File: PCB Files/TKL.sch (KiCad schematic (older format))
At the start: 486 parts, among them J1 USB_C, SW1 ESC, SW10 F9, SW100 RGUI_R2, SW101 RCTRL_R2, SW102 STEPPED_CAPS, SW103 RSHFT_175, SW104 Fn, SW105 BKSP_2U, SW11 F10, SW12 F11, SW13 F12, SW14 PRTSC, SW15 SCRLCK, SW16 PAUSE, SW17 GRV, SW18 1, SW19 2, SW2 F1, SW20 3, SW21 4, SW22 5, SW23 6, SW24 7, SW25 8, SW26 9, SW27 0, SW28 HIFEN, SW29 PLUS, SW3 F2, SW30 BCKSLSH, SW31 DEL, SW32 INS, SW33 HOME, SW34 PGUP, SW35 TAB, SW36 Q, SW37 W, SW38 E, SW39 R, SW4 F3, SW40 T, SW41 Y, SW42 U, SW43 I, SW44 O, SW45 P, SW46 LBRACES, SW47 RBRACES, SW48 BKSP_150, SW49 DEL, SW5 F4, SW50 END, SW51 PGDN, SW52 CAPS, SW53 A, SW54 S, SW55 D, SW56 F, SW57 G, SW58 H, SW59 J, SW6 F5, SW60 K, SW61 L, SW62 :, SW63 QUOTE, SW64 ENTER, SW65 LSHFT, SW66 Z, SW67 X, SW68 C, SW69 V, SW7 F6, SW70 B, SW71 N, SW72 M, SW73 <,, SW74 .>, SW75 /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

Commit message: Added TGB fourth row to schematic
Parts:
- added C52, C53, C54, C55, C56, C57, C58, C59, C60, C61, C62, C63, C64, C65: 100nF, Capacitor_SMD:C_0805_2012Metric, symbol Device:C_Small
- added L52, L53, L54, L55, L56, L57, L58, L59, L60, L61, L62, L63, L64, L65: LED_BGRA, acheron_Components:LED_RGB_SMD_6028_2.8x3.5mm_Round, symbol Device:LED_BGRA
- added R52, R53, R54, R55, R56, R57, R58, R59, R60, R61, R62, R63, R64, R65: 100R, Resistor_SMD:R_0805_2012Metric, symbol Device:R_Small
- added RD52, RD53, RD54, RD55, RD56, RD57, RD58, RD59, RD60, RD61, RD62, RD63, RD64, RD65: 33R, Resistor_SMD:R_0805_2012Metric, symbol Device:R_Small
- added U52, U53, U54, U55, U56, U57, U58, U59, U60, U61, U62, U63, U64, U65: WS2811M, acheron_Components:MSOP-8-1EP_3x3mm_P0.65mm_EP1.68x1.88mm, symbol acheronSymbols:WS2811M
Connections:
- net 5V: now also L52.4 (A), L53.4 (A), L54.4 (A), L55.4 (A), L56.4 (A), L57.4 (A), L58.4 (A), L59.4 (A), L60.4 (A), L61.4 (A), L62.4 (A), L63.4 (A), L64.4 (A), L65.4 (A), R52.1, R53.1, R54.1, R55.1, R56.1, R57.1, R58.1, R59.1, R60.1, R61.1, R62.1, R63.1, R64.1, R65.1
- net GND: now also C52.2, C53.2, C54.2, C55.2, C56.2, C57.2, C58.2, C59.2, C60.2, C61.2, C62.2, C63.2, C64.2, C65.2, U52.4 (GND), U52.9 (GND), U53.4 (GND), U53.9 (GND), U54.4 (GND), U54.9 (GND), U55.4 (GND), U55.9 (GND), U56.4 (GND), U56.9 (GND), U57.4 (GND), U57.9 (GND), U58.4 (GND), U58.9 (GND), U59.4 (GND), U59.9 (GND), U60.4 (GND), U60.9 (GND), U61.4 (GND), U61.9 (GND), U62.4 (GND), U62.9 (GND), U63.4 (GND), U63.9 (GND), U64.4 (GND), U64.9 (GND), U65.4 (GND), U65.9 (GND)
- net at U51.5 (DO): now also RD65.2
- new net: L65.3 (RK), U65.1 (OUTR)
- new net: L65.2 (GK), U65.2 (OUTG)
- new net: L65.1 (BK), U65.3 (OUTB)
- new net: RD64.2, U65.5 (DO)
- new net: RD65.1, U65.6 (DIN)
- new net: C65.1, R65.2, U65.8 (VDD)
- new net: L64.3 (RK), U64.1 (OUTR)
- new net: L64.2 (GK), U64.2 (OUTG)
- new net: L64.1 (BK), U64.3 (OUTB)
- new net: RD63.2, U64.5 (DO)
- new net: RD64.1, U64.6 (DIN)
- new net: C64.1, R64.2, U64.8 (VDD)
- new net: L63.3 (RK), U63.1 (OUTR)
- new net: L63.2 (GK), U63.2 (OUTG)
- new net: L63.1 (BK), U63.3 (OUTB)
- new net: RD62.2, U63.5 (DO)
- new net: RD63.1, U63.6 (DIN)
- new net: C63.1, R63.2, U63.8 (VDD)
- new net: RD62.1, U62.6 (DIN)
- new net: L62.3 (RK), U62.1 (OUTR)
- new net: L62.2 (GK), U62.2 (OUTG)
- new net: L62.1 (BK), U62.3 (OUTB)
- new net: RD61.2, U62.5 (DO)
- new net: C62.1, R62.2, U62.8 (VDD)
- new net: RD61.1, U61.6 (DIN)
- new net: L61.3 (RK), U61.1 (OUTR)
- new net: L61.2 (GK), U61.2 (OUTG)
- new net: L61.1 (BK), U61.3 (OUTB)
- new net: RD60.2, U61.5 (DO)
- new net: C61.1, R61.2, U61.8 (VDD)
- new net: RD52.1, U53.5 (DO)
- new net: RD52.2, U52.6 (DIN)
- new net: L52.3 (RK), U52.1 (OUTR)
- new net: L52.2 (GK), U52.2 (OUTG)
- new net: L52.1 (BK), U52.3 (OUTB)
- new net: C52.1, R52.2, U52.8 (VDD)
- new net: RD53.1, U53.6 (DIN)
- new net: RD53.2, U54.5 (DO)
- new net: L53.3 (RK), U53.1 (OUTR)
- new net: L53.2 (GK), U53.2 (OUTG)
- new net: L53.1 (BK), U53.3 (OUTB)
- new net: C53.1, R53.2, U53.8 (VDD)
- new net: RD54.1, U54.6 (DIN)
- new net: RD54.2, U55.5 (DO)
- new net: L54.3 (RK), U54.1 (OUTR)
- new net: L54.2 (GK), U54.2 (OUTG)
- new net: L54.1 (BK), U54.3 (OUTB)
- new net: C54.1, R54.2, U54.8 (VDD)
- new net: RD55.1, U55.6 (DIN)
- new net: RD55.2, U56.5 (DO)
- new net: L55.3 (RK), U55.1 (OUTR)
- new net: L55.2 (GK), U55.2 (OUTG)
- new net: L55.1 (BK), U55.3 (OUTB)
- new net: C55.1, R55.2, U55.8 (VDD)
- new net: RD56.1, U56.6 (DIN)
- new net: RD56.2, U57.5 (DO)
- new net: L56.3 (RK), U56.1 (OUTR)
- new net: L56.2 (GK), U56.2 (OUTG)
- new net: L56.1 (BK), U56.3 (OUTB)
- new net: C56.1, R56.2, U56.8 (VDD)
- new net: RD57.1, U57.6 (DIN)
- new net: RD57.2, U58.5 (DO)
- new net: L57.3 (RK), U57.1 (OUTR)
- new net: L57.2 (GK), U57.2 (OUTG)
- new net: L57.1 (BK), U57.3 (OUTB)
- new net: C57.1, R57.2, U57.8 (VDD)
- new net: C59.1, R59.2, U59.8 (VDD)
- new net: L59.1 (BK), U59.3 (OUTB)
- new net: L59.2 (GK), U59.2 (OUTG)
- new net: L59.3 (RK), U59.1 (OUTR)
- new net: RD58.2, U59.5 (DO)
- new net: RD59.1, U59.6 (DIN)
- new net: RD59.2, U60.5 (DO)
- new net: RD60.1, U60.6 (DIN)
- new net: L60.3 (RK), U60.1 (OUTR)
- new net: L60.2 (GK), U60.2 (OUTG)
- new net: L60.1 (BK), U60.3 (OUTB)
- new net: C60.1, R60.2, U60.8 (VDD)
- new net: RD58.1, U58.6 (DIN)
- new net: L58.3 (RK), U58.1 (OUTR)
- new net: L58.2 (GK), U58.2 (OUTG)
- new net: L58.1 (BK), U58.3 (OUTB)
- new net: C58.1, R58.2, U58.8 (VDD)

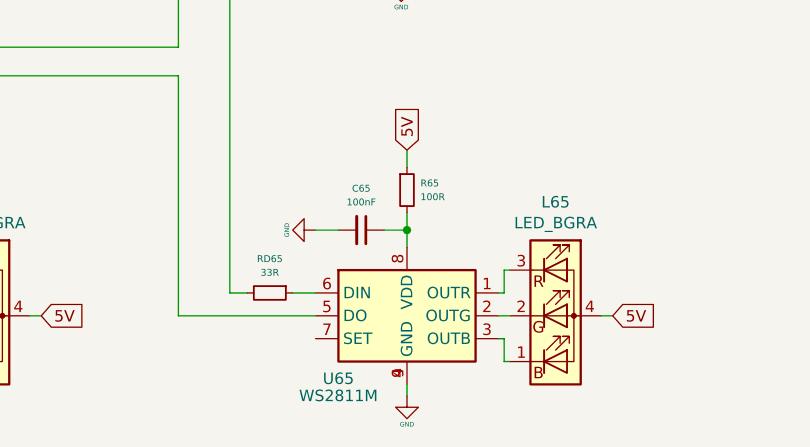
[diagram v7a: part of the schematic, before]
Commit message: Placed RGB LEDs and controllers of 4th row
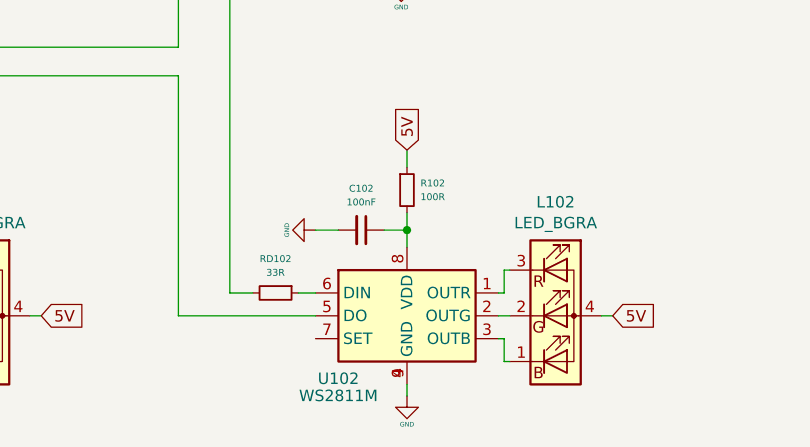
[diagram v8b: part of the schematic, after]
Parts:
- removed C65: 100nF, Capacitor_SMD:C_0805_2012Metric, symbol Device:C_Small
- removed L65: LED_BGRA, acheron_Components:LED_RGB_SMD_6028_2.8x3.5mm_Round, symbol Device:LED_BGRA
- removed R65: 100R, Resistor_SMD:R_0805_2012Metric, symbol Device:R_Small
- removed RD65: 33R, Resistor_SMD:R_0805_2012Metric, symbol Device:R_Small
- removed U65: WS2811M, acheron_Components:MSOP-8-1EP_3x3mm_P0.65mm_EP1.68x1.88mm, symbol acheronSymbols:WS2811M
- added C102: 100nF, Capacitor_SMD:C_0805_2012Metric, symbol Device:C_Small
- added L102: LED_BGRA, acheron_Components:LED_RGB_SMD_6028_2.8x3.5mm_Round, symbol Device:LED_BGRA
- added R102: 100R, Resistor_SMD:R_0805_2012Metric, symbol Device:R_Small
- added RD102: 33R, Resistor_SMD:R_0805_2012Metric, symbol Device:R_Small
- added U102: WS2811M, acheron_Components:MSOP-8-1EP_3x3mm_P0.65mm_EP1.68x1.88mm, symbol acheronSymbols:WS2811M
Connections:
- net 5V: now also L102.4 (A), R102.1
- net GND: now also C102.2, U102.4 (GND), U102.9 (GND)
- net at RD64.2: now also U102.5 (DO)
- net at U51.5 (DO): now also RD102.2
- new net: L102.3 (RK), U102.1 (OUTR)
- new net: L102.2 (GK), U102.2 (OUTG)
- new net: L102.1 (BK), U102.3 (OUTB)
- new net: RD102.1, U102.6 (DIN)
- new net: C102.1, R102.2, U102.8 (VDD)
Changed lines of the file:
@@
-$EndComp
-Wire Wire Line
-	42325 18375 42325 18325
-$Comp
-L power:GND #PWR092
-U 1 1 60BBF29D
-P 42325 18375
-F 0 "#PWR092" H 42325 18125 50  0001 C CNN
-F 1 "GND" H 42325 18250 20  0000 C CNN
-F 2 "" H 42325 18375 50  0001 C CNN
-F 3 "" H 42325 18375 50  0001 C CNN
-	1    42325 18375
-	1    0    0    -1
-$EndComp
-Text GLabel 42325 17300 1    50   Input ~ 0
-5V
-Wire Wire Line
-	43225 18025 43175 18025
-Text GLabel 43225 18025 2    50   Input ~ 0
-5V
-Wire Wire Line
-	42775 18025 42725 18025
-Wire Wire Line
-	42750 18225 42775 18225
-Wire Wire Line
-	42750 18125 42750 18225
-Wire Wire Line
-	42725 18125 42750 18125
-Wire Wire Line
-	42750 17925 42725 17925
-Wire Wire Line
-	42750 17825 42750 17925
-Wire Wire Line
-	42775 17825 42750 17825
-$Comp
-L acheronSymbols:WS2811M U65
-U 1 1 60BBF2AD
-P 42325 18025
-F 0 "U65" H 42025 17750 50  0000 C CNN
-F 1 "WS2811M" H 42025 17675 50  0000 C CNN
-F 2 "acheron_Components:MSOP-8-1EP_3x3mm_P0.65mm_EP1.68x1.88mm" H 42025 18175 50  0001 C CNN
-F 3 "https://cdn-shop.adafruit.com/datasheets/WS2811.pdf" H 42125 18275 50  0001 C CNN
-	1    42325 18025
-	1    0    0    -1
-$EndComp
-$Comp
-L Device:LED_BGRA L65
-U 1 1 60BBF2B3
-P 42975 18025
-F 0 "L65" H 42975 18522 50  0000 C CNN
-F 1 "LED_BGRA" H 42975 18431 50  0000 C CNN
-F 2 "acheron_Components:LED_RGB_SMD_6028_2.8x3.5mm_Round" H 42975 17975 50  0001 C CNN
-F 3 "~" H 42975 17975 50  0001 C CNN
-	1    42975 18025
-	1    0    0    -1
-$EndComp
-$Comp
-L Device:R_Small R65
-U 1 1 60BBF2B9
-P 42325 17475
-F 0 "R65" H 42384 17505 30  0000 L CNN
-F 1 "100R" H 42384 17445 30  0000 L CNN
-F 2 "Resistor_SMD:R_0805_2012Metric" H 42325 17475 50  0001 C CNN
-F 3 "~" H 42325 17475 50  0001 C CNN
-	1    42325 17475
-	1    0    0    -1
-$EndComp
-$Comp
-L Device:C_Small C65
-U 1 1 60BBF2BF
-P 42125 17650
-F 0 "C65" V 41943 17650 30  0000 C CNN
-F 1 "100nF" V 42003 17650 30  0000 C CNN
-F 2 "Capacitor_SMD:C_0805_2012Metric" H 42125 17650 50  0001 C CNN
-F 3 "~" H 42125 17650 50  0001 C CNN
-	1    42125 17650
-	0    1    1    0
-$EndComp
-Wire Wire Line
-	42325 17650 42225 17650
-Wire Wire Line
-	42025 17650 41925 17650
-Wire Wire Line
-	42325 17300 42325 17375
-Wire Wire Line
-	42325 17575 42325 17650
-Connection ~ 42325 17650
-Wire Wire Line
-	42325 17650 42325 17725
-$Comp
-L power:GND #PWR091
-U 1 1 60BBF2CB
-P 41925 17650
-F 0 "#PWR091" H 41925 17400 50  0001 C CNN
-F 1 "GND" H 41925 17525 20  0000 C CNN
-F 2 "" H 41925 17650 50  0001 C CNN
-F 3 "" H 41925 17650 50  0001 C CNN
-	1    41925 17650
-	0    1    1    0
 $EndComp
 Wire Wire Line
@@
 Wire Wire Line
 	41325 18025 41925 18025
-Wire Wire Line
-	41550 17925 41625 17925
 Wire Wire Line
 	41325 16975 41325 18025
@@
 	9850 18375 9850 18325
 Wire Wire Line
-	41825 17925 41925 17925
-Wire Wire Line
 	9400 17925 9450 17925
 Wire Wire Line
@@
 	0    1    1    0
 $EndComp
-$Comp
-L Device:R_Small RD65
-U 1 1 60BBF622
-P 41725 17925
-F 0 "RD65" V 41576 17925 30  0000 C CNN
-F 1 "33R" V 41636 17925 30  0000 C CNN
-F 2 "Resistor_SMD:R_0805_2012Metric" H 41725 17925 50  0001 C CNN
-F 3 "~" H 41725 17925 50  0001 C CNN
-	1    41725 17925
+Wire Wire Line
+	8875 18025 9450 18025
+Wire Wire Line
+	42325 18375 42325 18325
+$Comp
+L power:GND #PWR0162
+U 1 1 5DCF0222
+P 42325 18375
+F 0 "#PWR0162" H 42325 18125 50  0001 C CNN
+F 1 "GND" H 42325 18250 20  0000 C CNN
+F 2 "" H 42325 18375 50  0001 C CNN
+F 3 "" H 42325 18375 50  0001 C CNN
+	1    42325 18375
+	1    0    0    -1
+$EndComp
+Text GLabel 42325 17300 1    50   Input ~ 0
+5V
+Wire Wire Line
+	43225 18025 43175 18025
+Text GLabel 43225 18025 2    50   Input ~ 0
+5V
+Wire Wire Line
+	42775 18025 42725 18025
+Wire Wire Line
+	42750 18225 42775 18225
+Wire Wire Line
+	42750 18125 42750 18225
+Wire Wire Line
+	42725 18125 42750 18125
+Wire Wire Line
+	42750 17925 42725 17925
+Wire Wire Line
+	42750 17825 42750 17925
+Wire Wire Line
+	42775 17825 42750 17825
+$Comp
+L acheronSymbols:WS2811M U102
+U 1 1 5DCF0232
+P 42325 18025
+F 0 "U102" H 42025 17750 50  0000 C CNN
+F 1 "WS2811M" H 42025 17675 50  0000 C CNN
+F 2 "acheron_Components:MSOP-8-1EP_3x3mm_P0.65mm_EP1.68x1.88mm" H 42025 18175 50  0001 C CNN
+F 3 "https://cdn-shop.adafruit.com/datasheets/WS2811.pdf" H 42125 18275 50  0001 C CNN
+	1    42325 18025
+	1    0    0    -1
+$EndComp
+$Comp
+L Device:LED_BGRA L102
+U 1 1 5DCF0238
+P 42975 18025
+F 0 "L102" H 42975 18522 50  0000 C CNN
+F 1 "LED_BGRA" H 42975 18431 50  0000 C CNN
+F 2 "acheron_Components:LED_RGB_SMD_6028_2.8x3.5mm_Round" H 42975 17975 50  0001 C CNN
+F 3 "~" H 42975 17975 50  0001 C CNN
+	1    42975 18025
+	1    0    0    -1
+$EndComp
+$Comp
+L Device:R_Small R102
+U 1 1 5DCF023E
+P 42325 17475
+F 0 "R102" H 42384 17505 30  0000 L CNN
+F 1 "100R" H 42384 17445 30  0000 L CNN
+F 2 "Resistor_SMD:R_0805_2012Metric" H 42325 17475 50  0001 C CNN
+F 3 "~" H 42325 17475 50  0001 C CNN
+	1    42325 17475
+	1    0    0    -1
+$EndComp
+$Comp
+L Device:C_Small C102
+U 1 1 5DCF0244
+P 42125 17650
+F 0 "C102" V 41943 17650 30  0000 C CNN
+F 1 "100nF" V 42003 17650 30  0000 C CNN
+F 2 "Capacitor_SMD:C_0805_2012Metric" H 42125 17650 50  0001 C CNN
+F 3 "~" H 42125 17650 50  0001 C CNN
+	1    42125 17650
+	0    1    1    0
+$EndComp
+Wire Wire Line
+	42325 17650 42225 17650
+Wire Wire Line
+	42025 17650 41925 17650
+Wire Wire Line
+	42325 17300 42325 17375
+Wire Wire Line
+	42325 17575 42325 17650
+Connection ~ 42325 17650
+Wire Wire Line
+	42325 17650 42325 17725
+$Comp
+L power:GND #PWR0163
+U 1 1 5DCF0250
+P 41925 17650
+F 0 "#PWR0163" H 41925 17400 50  0001 C CNN
+F 1 "GND" H 41925 17525 20  0000 C CNN
+F 2 "" H 41925 17650 50  0001 C CNN
+F 3 "" H 41925 17650 50  0001 C CNN
+	1    41925 17650
+	0    1    1    0
+$EndComp
+Wire Wire Line
+	41850 17925 41925 17925
+Wire Wire Line
+	41650 17925 41550 17925
+$Comp
+L Device:R_Small RD102
+U 1 1 5DCF025D
+P 41750 17925
+F 0 "RD102" V 41601 17925 30  0000 C CNN
+F 1 "33R" V 41661 17925 30  0000 C CNN
+F 2 "Resistor_SMD:R_0805_2012Metric" H 41750 17925 50  0001 C CNN
+F 3 "~" H 41750 17925 50  0001 C CNN
+	1    41750 17925
 	0    1    1    0
 $EndComp
 Wire Wire Line
 	41550 16200 41550 17925
-Wire Wire Line
-	8875 18025 9450 18025
 $EndSCHEMATC
